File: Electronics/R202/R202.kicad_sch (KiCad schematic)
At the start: 57 parts, among them J1 Screw_Terminal_01x09, J2 RC 6CH Receiver, J5 Screw_Terminal_01x06, J6 Screw_Terminal_01x04, J7 Screw_Terminal_01x10, J8 Screw_Terminal_01x09, SW1 SW_SPST, U1 LoRa-SX1262, U2 RP2040-Zero (w/ extra breakou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, U3 Adafruit GPS (MTK3339)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

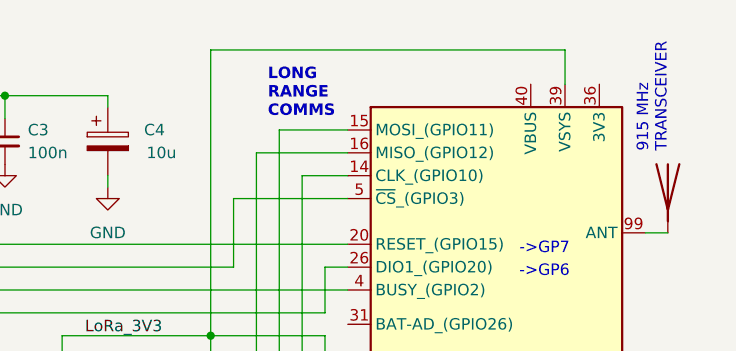
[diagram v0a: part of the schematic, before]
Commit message: Error fix, power net to LoRa module moved from incorrect pin 39 to correct pin 36
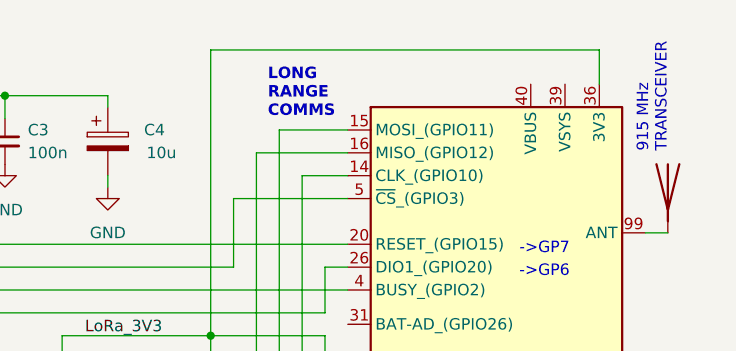
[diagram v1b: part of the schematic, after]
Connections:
- net SONAR-POWER-3V3: now also U1.36 (3V3); no longer U1.39 (VSYS)
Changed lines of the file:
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@@
   (title_block
     (title "Roverling MK II Controller")
-    (date "2023-09-21")
-    (rev "2.02")
+    (date "2023-11-12")
+    (rev "2.03")
   )
   (junction (at 234.95 133.35) (diameter 0) (color 0 0 0 0)
@@
     (stroke (width 0) (type default) (color 0 0 0 0))
   )
-  (wire (pts (xy 228.6 7.62) (xy 267.97 7.62))
+  (wire (pts (xy 228.6 7.62) (xy 271.78 7.62))
     (stroke (width 0) (type default) (color 0 0 0 0))
   )
@@
     (stroke (width 0) (type default) (color 0 0 0 0))
   )
+  (wire (pts (xy 271.78 7.62) (xy 271.78 11.43))
+    (stroke (width 0) (type default) (color 0 0 0 0))
+  )
   (wire (pts (xy 172.72 10.16) (xy 172.72 12.7))
     (stroke (width 0) (type default) (color 0 0 0 0))
@@
     (stroke (width 0) (type default) (color 0 0 0 0))
   )
-  (wire (pts (xy 267.97 11.43) (xy 267.97 7.62))
-    (stroke (width 0) (type default) (color 0 0 0 0))
-  )
